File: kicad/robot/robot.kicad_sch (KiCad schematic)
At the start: 55 parts, among them U1 DNP, U10 BM03BPASS1TFTLFSN, U7 AP2502KTR-G1

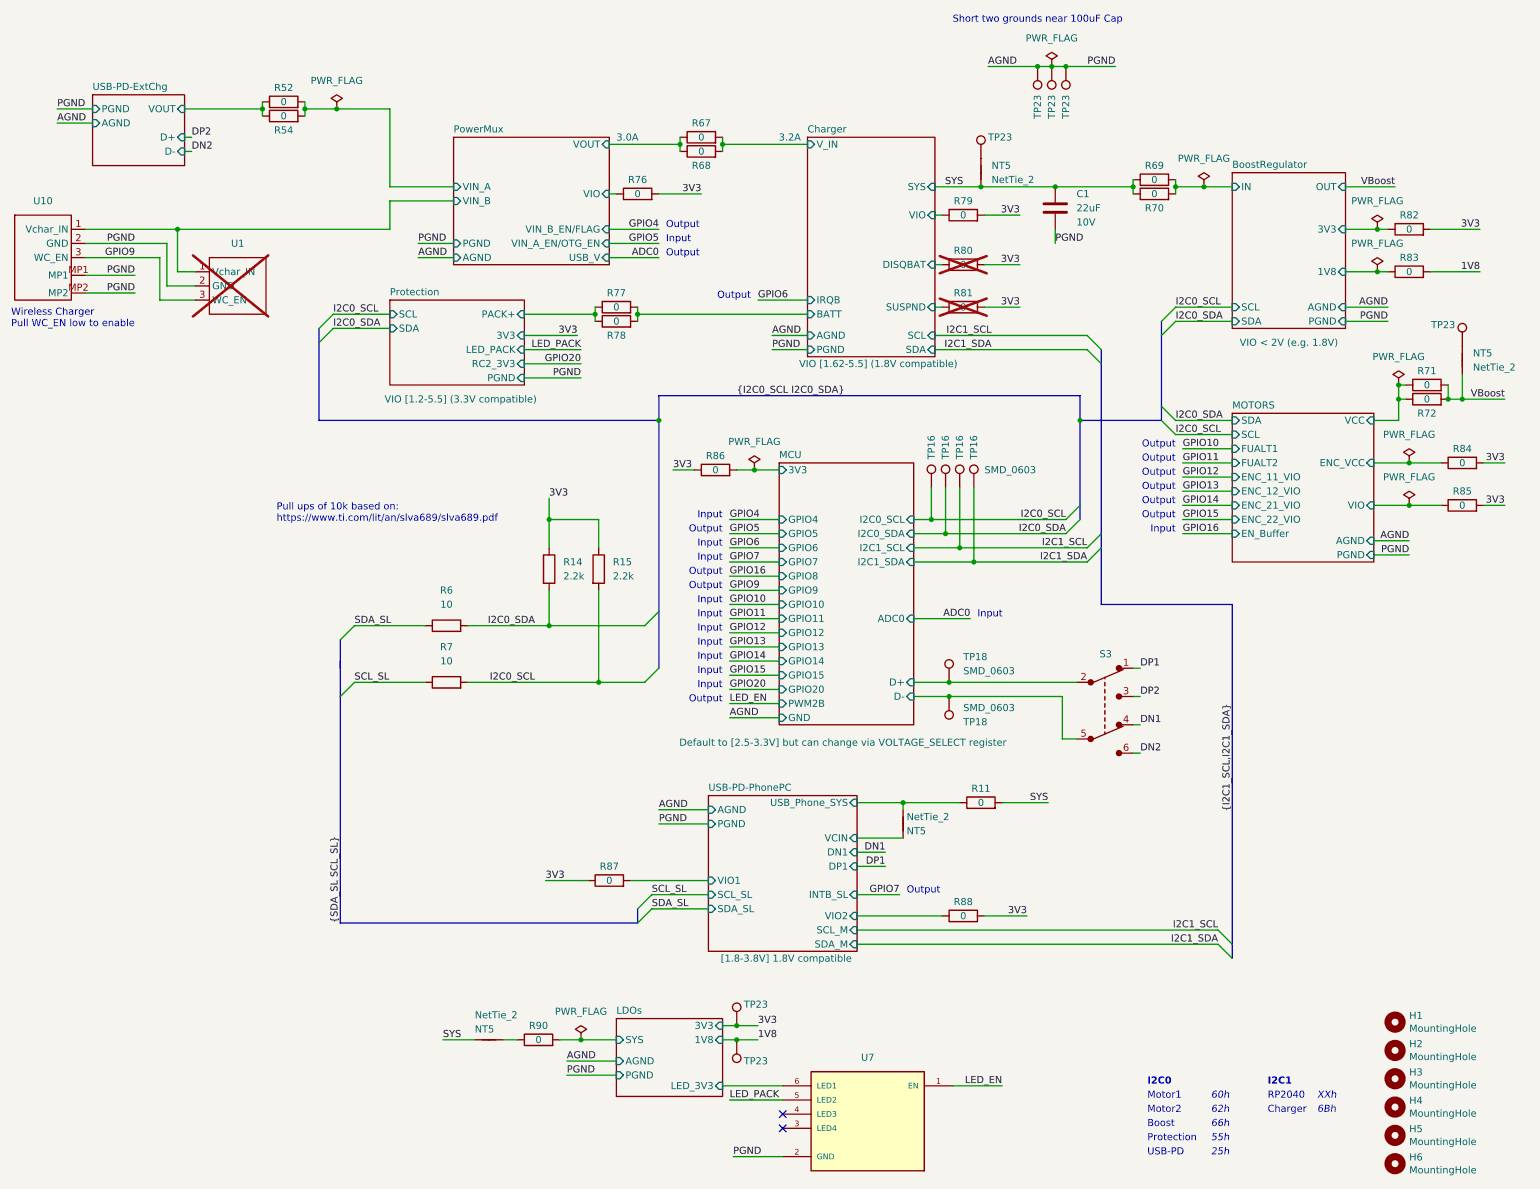
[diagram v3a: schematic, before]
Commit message: wireless receiver schematic finished (other than BOM)
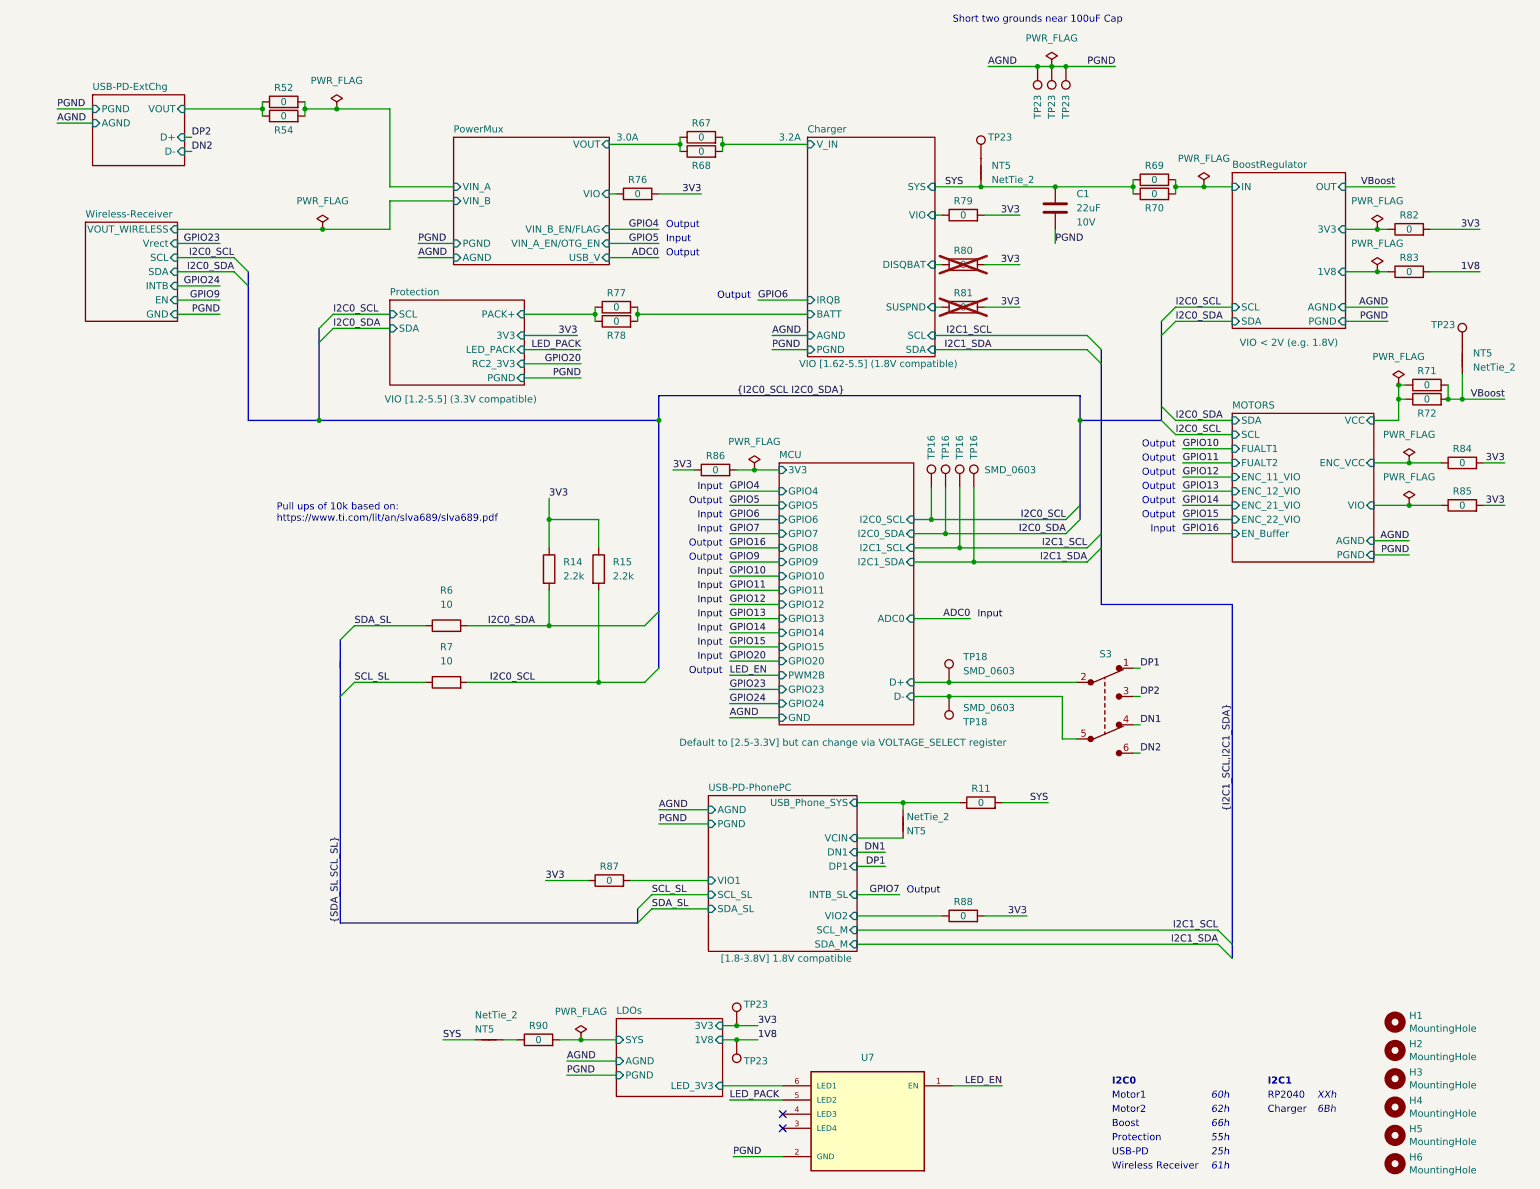
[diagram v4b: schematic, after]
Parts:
- removed U1: DNP, symbol robot:WRM483265-10F5-12V-G
- removed U10: BM03BPASS1TFTLFSN, robot:BM03BPASS1TFTLFSN, symbol robot:BM03BPASS1TFTLFSN
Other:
- added sheet Wireless-Receiver (Wireless-Receiver.kicad_sch)
- sheet MCU ports: added GPIO23, GPIO24; removed none
- note added: "61h"
- note added: "Wireless Receiver"
- note removed: "Wireless Charger Pull WC_EN low to enable"

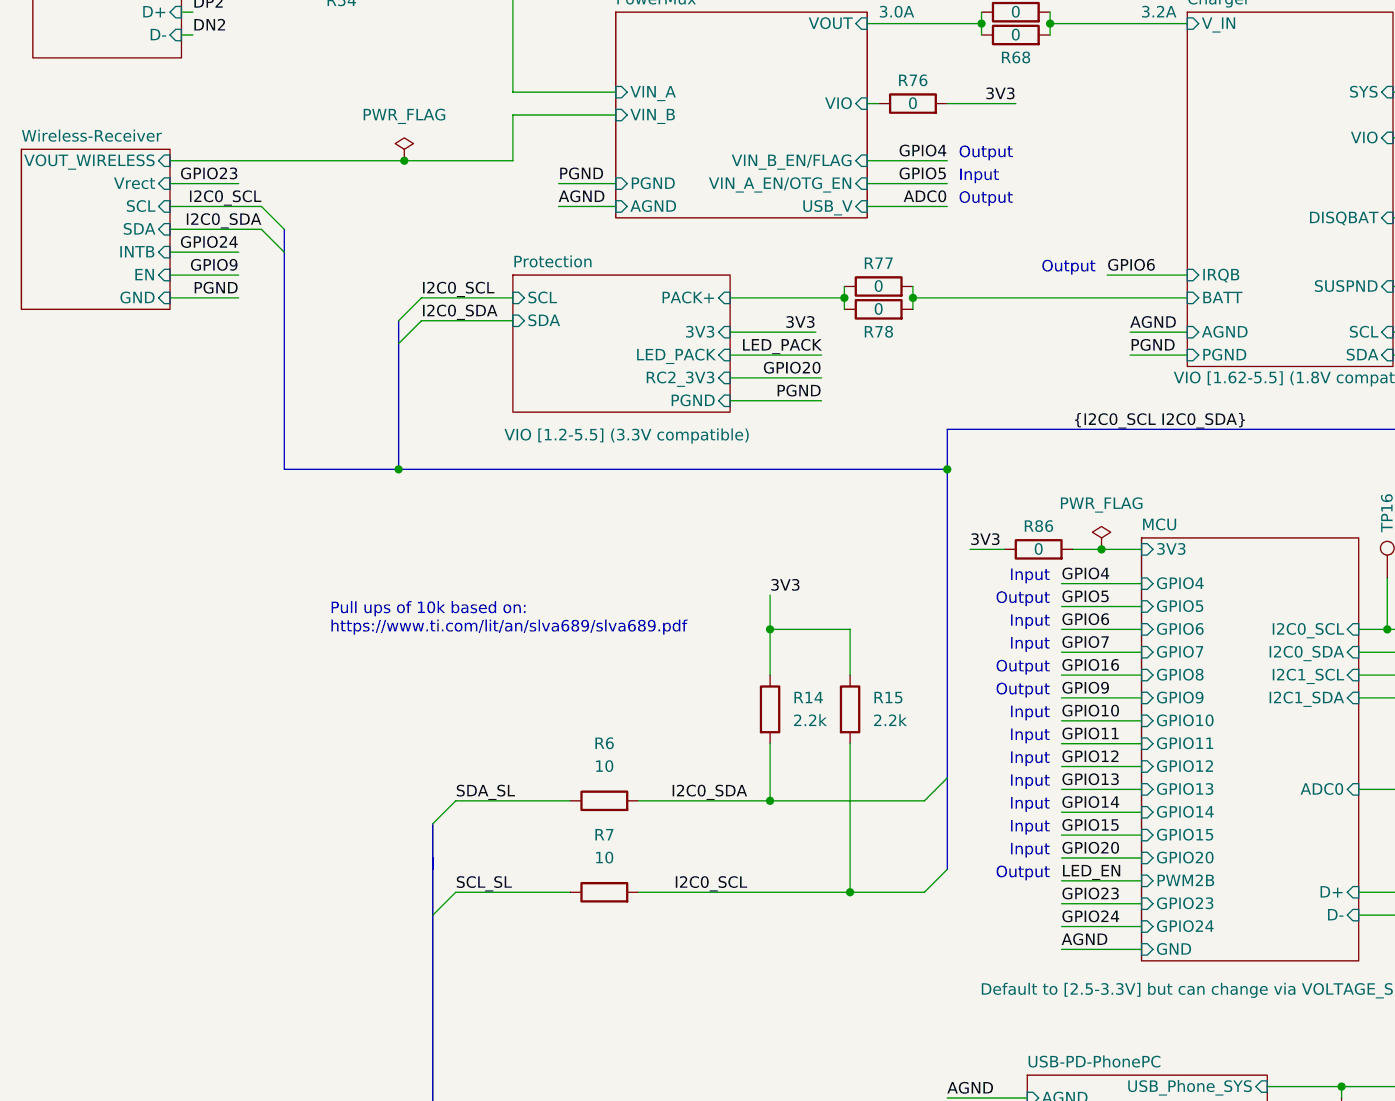
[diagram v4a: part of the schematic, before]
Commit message: Connected adc1 instead of gpio24 to vrect
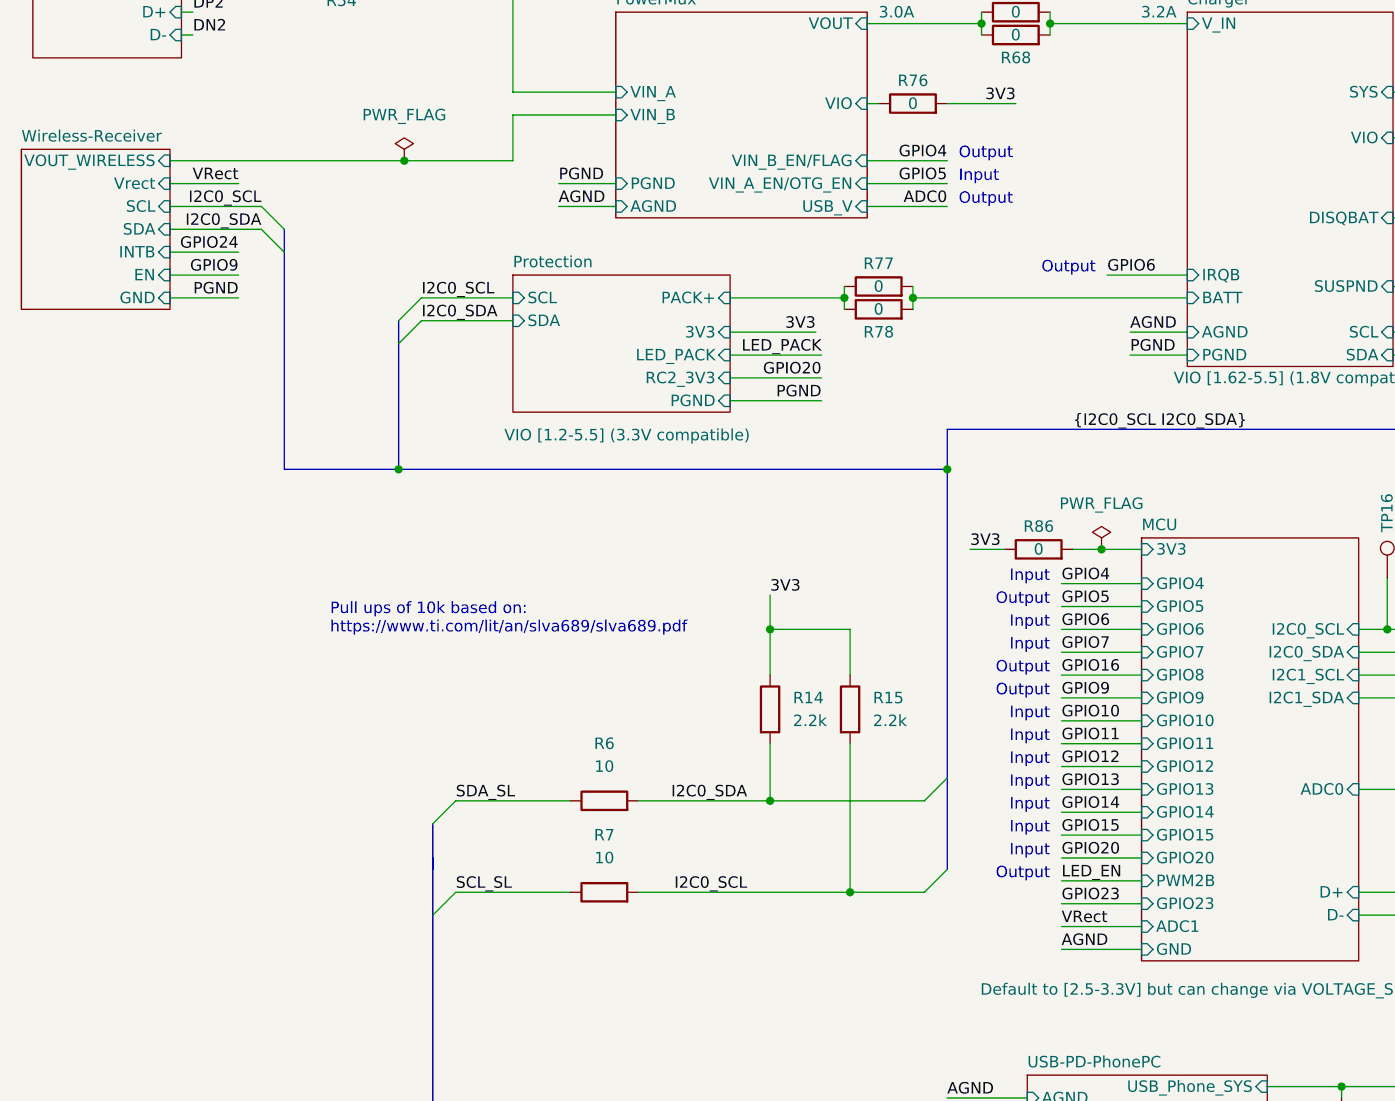
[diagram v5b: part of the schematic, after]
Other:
- sheet MCU ports: added ADC1; removed GPIO24
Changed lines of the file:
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@@
+    (effects (font (size 1.27 1.27)) (justify left bottom))
+  )
+  (label "VRect" (at 139.7 127 0) (fields_autoplaced)
     (effects (font (size 1.27 1.27)) (justify left bottom))
   )
@@
     (effects (font (size 1.27 1.27)) (justify left bottom))
   )
-  (label "GPIO24" (at 139.7 127 0) (fields_autoplaced)
-    (effects (font (size 1.27 1.27)) (justify left bottom))
-  )
   (label "SDA_SL" (at 72.39 113.03 0) (fields_autoplaced)
     (effects (font (size 1.27 1.27)) (justify left bottom))
@@
     (effects (font (size 1.27 1.27)) (justify left bottom))
   )
-  (label "GPIO23" (at 48.26 44.45 180) (fields_autoplaced)
+  (label "VRect" (at 48.26 44.45 180) (fields_autoplaced)
     (effects (font (size 1.27 1.27)) (justify right bottom))
   )
@@
       (effects (font (size 1.27 1.27)) (justify left))
     )
-    (pin "GPIO24" input (at 148.59 127 180)
-      (effects (font (size 1.27 1.27)) (justify left))
-    )
+    (pin "ADC1" input (at 148.59 127 180)
+      (effects (font (size 1.27 1.27)) (justify left))
+    )

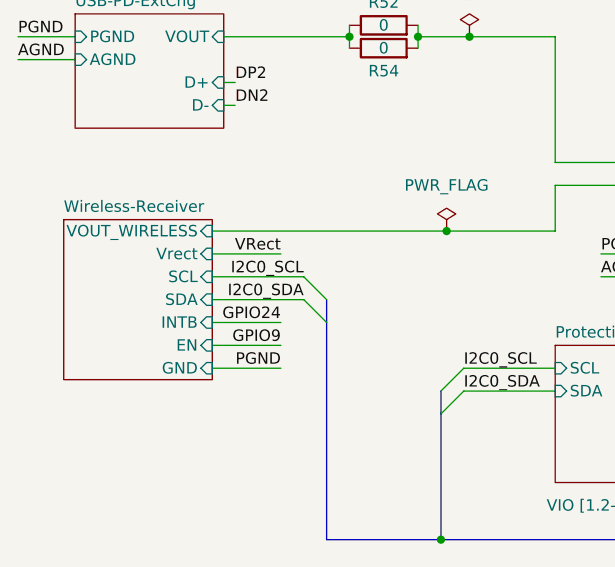
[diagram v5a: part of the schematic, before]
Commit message: Adding wireless charger circuit
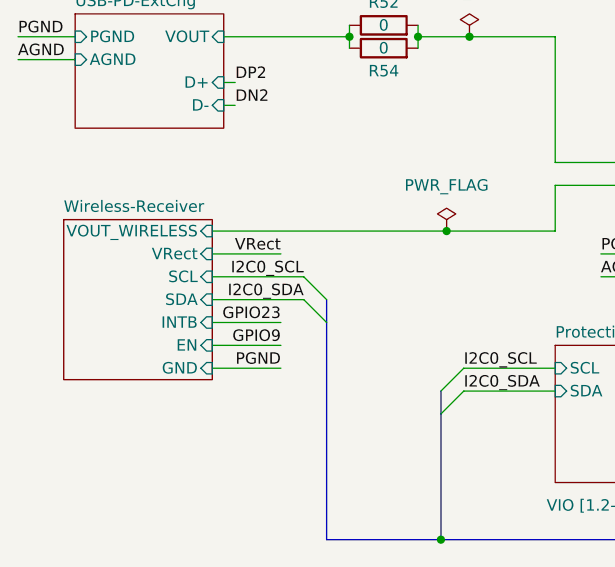
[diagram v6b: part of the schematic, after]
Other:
- sheet Wireless-Receiver ports: added VRect; removed Vrect
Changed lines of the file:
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@@
     (effects (font (size 1.27 1.27)) (justify right bottom))
   )
-  (label "GPIO24" (at 48.26 52.07 180) (fields_autoplaced)
+  (label "GPIO23" (at 48.26 52.07 180) (fields_autoplaced)
     (effects (font (size 1.27 1.27)) (justify right bottom))
   )
@@
       (effects (font (size 1.27 1.27)) (justify right))
     )
-    (pin "Vrect" input (at 40.64 44.45 0)
-      (effects (font (size 1.27 1.27)) (justify right))
-    )
     (pin "SDA" input (at 40.64 49.53 0)
       (effects (font (size 1.27 1.27)) (justify right))
@@
       (effects (font (size 1.27 1.27)) (justify right))
     )
+    (pin "VRect" input (at 40.64 44.45 0)
+      (effects (font (size 1.27 1.27)) (justify right))
+    )

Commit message: Updating stock on digikey parts delivered
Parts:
- R76, R79, R80, R81, R82, R83, R84, R85, R86, R87, R88, R90: Stock (none) -> 15
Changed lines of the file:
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@@
       (effects (font (size 1.27 1.27)) hide)
     )
-    (property "Stock" "" (at 105.41 187.325 0)
+    (property "Stock" "15" (at 105.41 187.325 0)
       (effects (font (size 1.27 1.27)) hide)
     )
@@
       (effects (font (size 1.27 1.27)) hide)
     )
-    (property "Stock" "" (at 181.61 165.1 0)
+    (property "Stock" "15" (at 181.61 165.1 0)
       (effects (font (size 1.27 1.27)) hide)
     )
@@
       (effects (font (size 1.27 1.27)) hide)
     )
-    (property "Stock" "" (at 271.145 83.82 0)
+    (property "Stock" "15" (at 271.145 83.82 0)
       (effects (font (size 1.27 1.27)) hide)
     )
@@
       (effects (font (size 1.27 1.27)) hide)
     )
-    (property "Stock" "" (at 181.61 48.26 0)
+    (property "Stock" "15" (at 181.61 48.26 0)
       (effects (font (size 1.27 1.27)) hide)
     )
@@
       (effects (font (size 1.27 1.27)) hide)
     )
-    (property "Stock" "" (at 181.61 39.37 0)
+    (property "Stock" "15" (at 181.61 39.37 0)
       (effects (font (size 1.27 1.27)) hide)
     )
@@
       (effects (font (size 1.27 1.27)) hide)
     )
-    (property "Stock" "" (at 261.62 49.53 0)
+    (property "Stock" "15" (at 261.62 49.53 0)
       (effects (font (size 1.27 1.27)) hide)
     )
@@
       (effects (font (size 1.27 1.27)) hide)
     )
-    (property "Stock" "" (at 271.145 91.44 0)
+    (property "Stock" "15" (at 271.145 91.44 0)
       (effects (font (size 1.27 1.27)) hide)
     )
@@
       (effects (font (size 1.27 1.27)) hide)
     )
-    (property "Stock" "" (at 181.61 55.88 0)
+    (property "Stock" "15" (at 181.61 55.88 0)
       (effects (font (size 1.27 1.27)) hide)
     )
@@
       (effects (font (size 1.27 1.27)) hide)
     )
-    (property "Stock" "" (at 123.19 35.56 0)
+    (property "Stock" "15" (at 123.19 35.56 0)
       (effects (font (size 1.27 1.27)) hide)
     )
@@
       (effects (font (size 1.27 1.27)) hide)
     )
-    (property "Stock" "" (at 118.11 158.75 0)
+    (property "Stock" "15" (at 118.11 158.75 0)
       (effects (font (size 1.27 1.27)) hide)
     )
@@
       (effects (font (size 1.27 1.27)) hide)
     )
-    (property "Stock" "" (at 137.16 85.09 0)
+    (property "Stock" "15" (at 137.16 85.09 0)
       (effects (font (size 1.27 1.27)) hide)
     )
@@
       (effects (font (size 1.27 1.27)) hide)
     )
-    (property "Stock" "" (at 261.62 41.91 0)
-      (effects (font (size 1.27 1.27)) hide)
-    )
+    (property "Stock" "15" (at 261.62 41.91 0)
+      (effects (font (size 1.27 1.27)) hide)
+    )

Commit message: Adding type field to all parts for pcbway
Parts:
- C1, R11, R14, R15, R52, R54, R6, R67, R68, R69, R7, R70, R71, R72, R76, R77, R78, R79, R80, R81, R82, R83, R84, R85, R86, R87, R88, R90, S3, TP16, TP18, U7: Type (none) -> SMD
- H1, H2, H3, H4, H5, H6, NT5: Type (none) -> DNP
- TP23: Type (none) -> THT
